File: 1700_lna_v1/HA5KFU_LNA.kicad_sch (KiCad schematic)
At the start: 17 parts, among them J1 Conn_Coaxial, J2 Conn_Coaxial, J3 Conn_01x02_Socket, U1 NCP163ASN330T1G, U2 QPL9547, U3 TFS1690

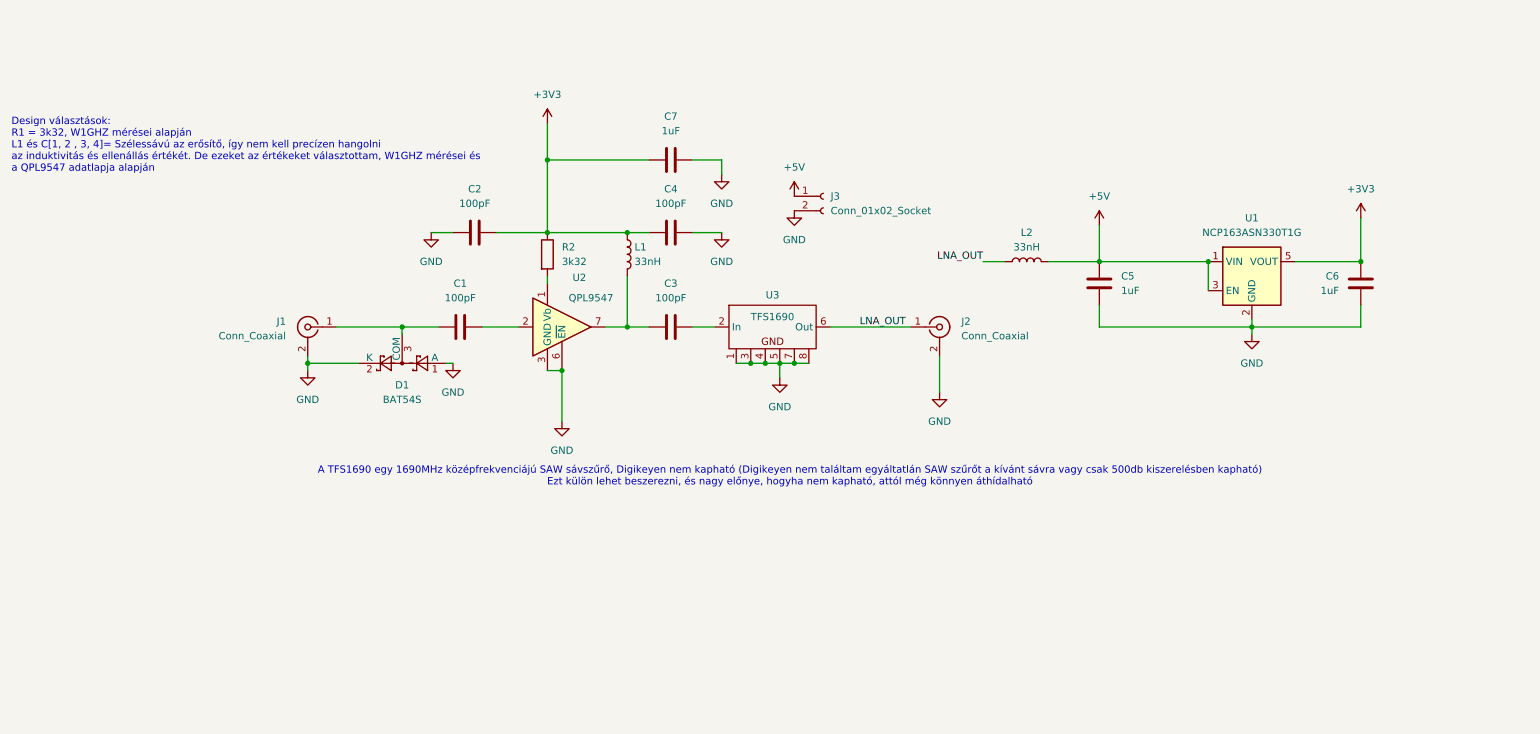
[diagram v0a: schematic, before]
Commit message: Added BOM, project file
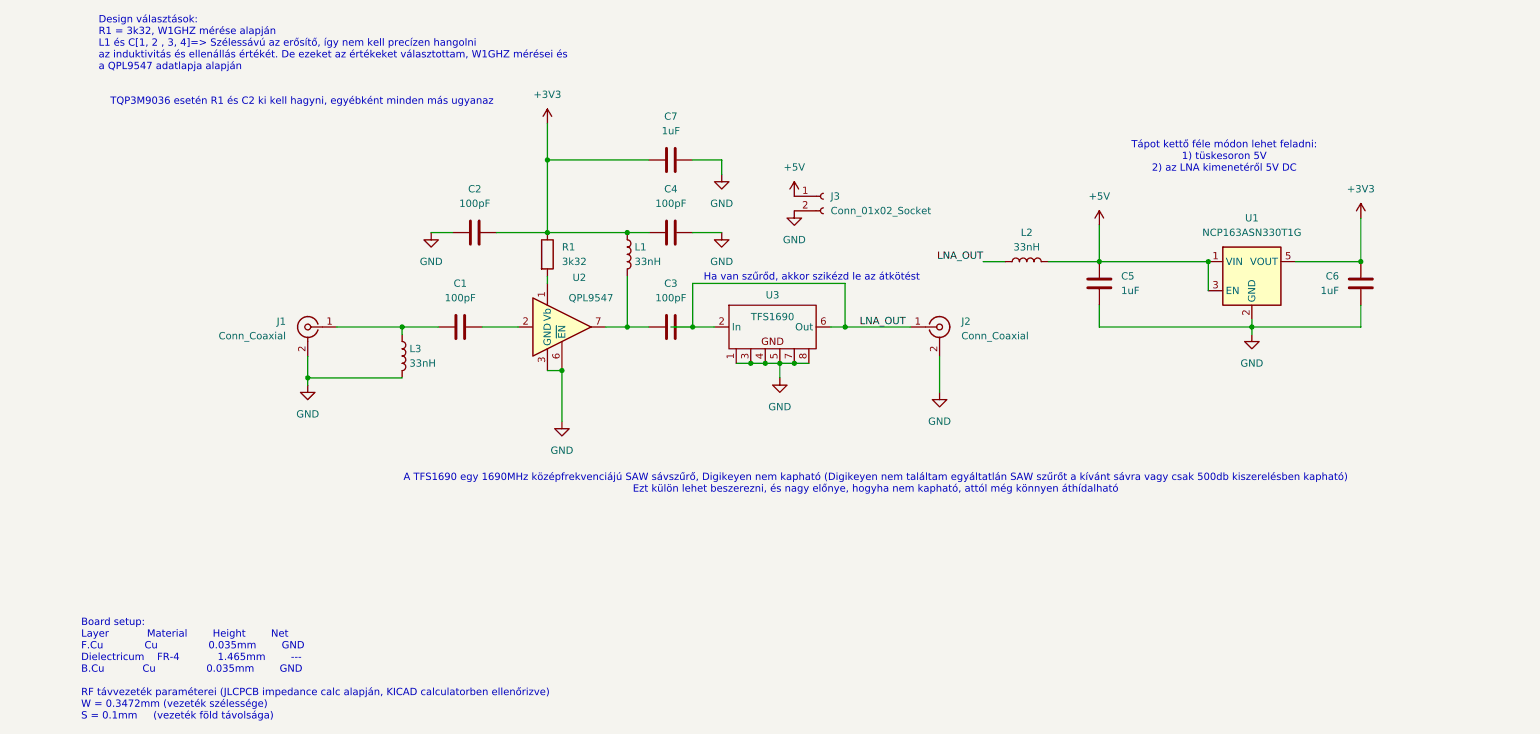
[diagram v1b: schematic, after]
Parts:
- removed D1: BAT54S, Package_TO_SOT_SMD:SOT-23, symbol Diode:BAT54S
- added L3: 33nH, Inductor_SMD:L_0402_1005Metric_Pad0.77x0.64mm_HandSolder, symbol Device:L
- J1: footprint Connector_Coaxial:SMA_Amphenol_132289_EdgeMount -> Connector_Coaxial:SMA_Amphenol_132134_Vertical
- J2: footprint Connector_Coaxial:SMA_Amphenol_132289_EdgeMount -> Connector_Coaxial:SMA_Amphenol_132291_Vertical
- U2, U3: now left out of the parts list
- renumbered R2 to R1
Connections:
- net GND: now also L3.2
- net LNA_OUT: now also C3.2, U3.2 (In)
- net at C1.1, J1.1 (In): now also L3.1
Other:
- note added: "Board setup: Layer Material Height Net F.Cu Cu 0.035mm GND Dielectricum FR-4 1.465mm --- B.Cu Cu 0.035mm GND RF távvezeték paraméterei (JLCPCB impedance calc alapján, KICAD calculatorben ellenőrizve) W = 0.3472mm (vezeték szélessége) S = 0.1mm (vezeték föld távolsága)"
- note added: "Design választások: R1 = 3k32, W1GHZ mérése alapján L1 és C[1, 2 , 3, 4]=> Szélessávú az erősítő, így nem kell precízen hangolni az induktivitás és ellenállás értékét. De ezeket az értékeket választottam, W1GHZ mérései és a QPL9547 adatlapja alapján"
- note added: "Ha van szűrőd, akkor szikézd le az átkötést"
- note added: "TQP3M9036 esetén R1 és C2 ki kell hagyni, egyébként minden más ugyanaz"
- note added: "Tápot kettő féle módon lehet feladni: 1) tüskesoron 5V 2) az LNA kimenetéről 5V DC"
- note removed: "Design választások: R1 = 3k32, W1GHZ mérései alapján L1 és C[1, 2 , 3, 4]= Szélessávú az erősítő, így nem kell precízen hangolni az induktivitás és ellenállás értékét. De ezeket az értékeket választottam, W1GHZ mérései és a QPL9547 adatlapja alapján"

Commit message: Adjusted 2 layer PCB design
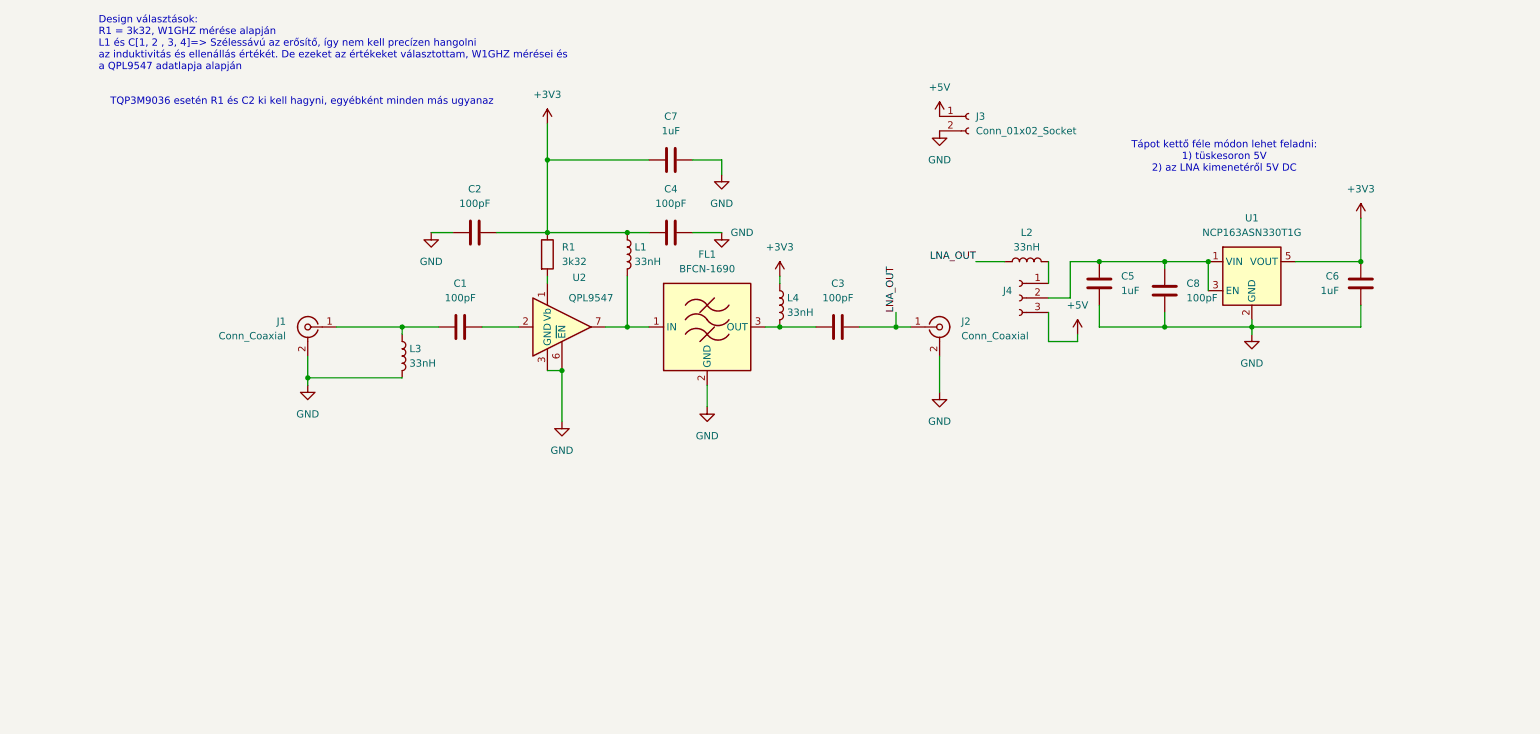
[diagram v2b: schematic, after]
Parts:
- removed U3: TFS1690, SAW_filt_lib:TFS1690, symbol SAW_filt_sym:TFS1690
- added C8: 100pF, Capacitor_SMD:C_0402_1005Metric_Pad0.74x0.62mm_HandSolder, symbol Device:C
- added FL1: BFCN-1690, Filter:Filter_Mini-Circuits_FV1206-1, symbol RF_Filter:BFCN-1690
- added J4: Conn_01x03_Socket, Connector_PinHeader_2.54mm:PinHeader_1x03_P2.54mm_Vertical, symbol Connector:Conn_01x03_Socket
- added L4: 33nH, Inductor_SMD:L_0402_1005Metric_Pad0.77x0.64mm_HandSolder, symbol Device:L
- J2: footprint Connector_Coaxial:SMA_Amphenol_132291_Vertical -> Connector_Coaxial:SMA_Amphenol_132134_Vertical
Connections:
- net +3V3: now also L4.1
- net +5V: now also J4.3 (Pin_3); no longer C5.1, L2.2, U1.1 (VIN), U1.3 (EN)
- net GND: now also C8.1, FL1.2 (GND), FL1.4 (GND), FL1.5 (GND), FL1.6 (GND)
- net at L1.2, U2.7: now also FL1.1 (IN); no longer C3.1
- new net: C3.1, FL1.3 (OUT), L4.2
- new net: J4.1 (Pin_1), L2.2
- new net: C5.1, C8.2, J4.2 (Pin_2), U1.1 (VIN), U1.3 (EN)
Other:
- note removed: "A TFS1690 egy 1690MHz középfrekvenciájú SAW sávszűrő, Digikeyen nem kapható (Digikeyen nem találtam egyáltatlán SAW szűrőt a kívánt sávra vagy csak 500db kiszerelésben kapható) Ezt külön lehet beszerezni, és nagy előnye, hogyha nem kapható, attól még könnyen áthídalható"
- note removed: "Board setup: Layer Material Height Net F.Cu Cu 0.035mm GND Dielectricum FR-4 1.465mm --- B.Cu Cu 0.035mm GND RF távvezeték paraméterei (JLCPCB impedance calc alapján, KICAD calculatorben ellenőrizve) W = 0.3472mm (vezeték szélessége) S = 0.1mm (vezeték föld távolsága)"
- note removed: "Ha van szűrőd, akkor szikézd le az átkötést"
- moved on the sheet: J3
